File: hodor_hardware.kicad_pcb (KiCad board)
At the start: 2 copper layers, 153.6 x 86 mm, 274 parts, among them J1 Screw_Terminal_01x02, J12 Conn_01x24_Pin, J13 Conn_01x24_Socket, J2 Screw_Terminal_01x06, J3 Screw_Terminal_01x03, J4 USB_C_Receptacle_USB2.0_16P, J5 Screw_Terminal_01x03, J6 Screw_Terminal_01x04, J7 Screw_Terminal_01x02, J8 Screw_Terminal_01x04, J9 Conn_01x04_Pin, K1 FINDER-32.21-x000, K2 FINDER-32.21-x000, Q1 SiS443DN, Q10 BC847BDW1, Q11 2V7002, Q2 BSS138DW, Q3 BSS138DW, Q4 IRLML9301, Q5 BSS138, Q6 BSS138DW, Q7 SiS443DN, Q9 IRLML9301, SW1 SW_RST, SW2 SW_BOOT, T1 GND, T10 V_{BUS}, T11 3V3, T12 5V, T13 5V, T14 V_{BUS}_SENSE, T15 I_SNS, T16 D_FB, T17 D_PWM2, T18 D_PWM1, T19 VC_OUT, T20 V_LDSNS, T21 SCL, T22 VC_CMP, T23 VC_REF, T24 SDA, T25 DRV_EN, T26 DRV_SF, T27 SF_Q, T28 SF_TRG, T29 SF_CLR, T30 ENC_B, T31 ENC_A, T32 GND, T33 3V3, T34 GND, T4 IN2, T5 IN1, T6 V_{DC}_SENSE, T7 IN3, T8 IN4, T9 V_{DC}, U1 ESP32-S3-WROOM-1_N8R2, U10 LM4040DBZ-2.5, U11 MCP6561x-LT, U12 ZXTR2105F, U14 ACS722xLCTR-10AB, U15 TPS2116DRL, U16 MCP23S08-xML, U17 SSD1306, U18 MC33HB2002, U2 TLV62569DBV, U3 74LVC2G14, U4 74LVC2G14, U5 TPS54240DRC, U6 MAX811SEUS-T, U7 74LVC2G14, U8 74LVC1G123, U9 24LC256

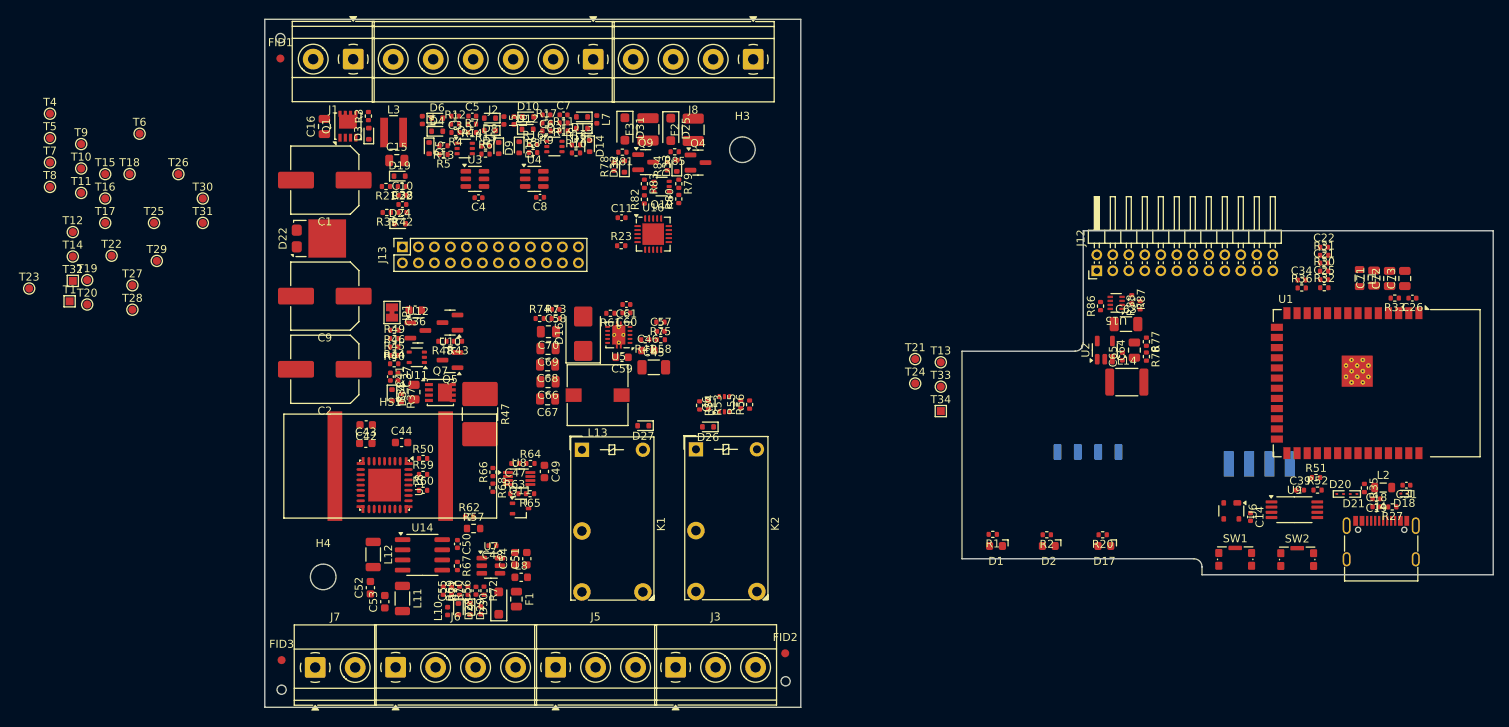
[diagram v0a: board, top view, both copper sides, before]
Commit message: Simplified design (Old version switched to hodor-max)
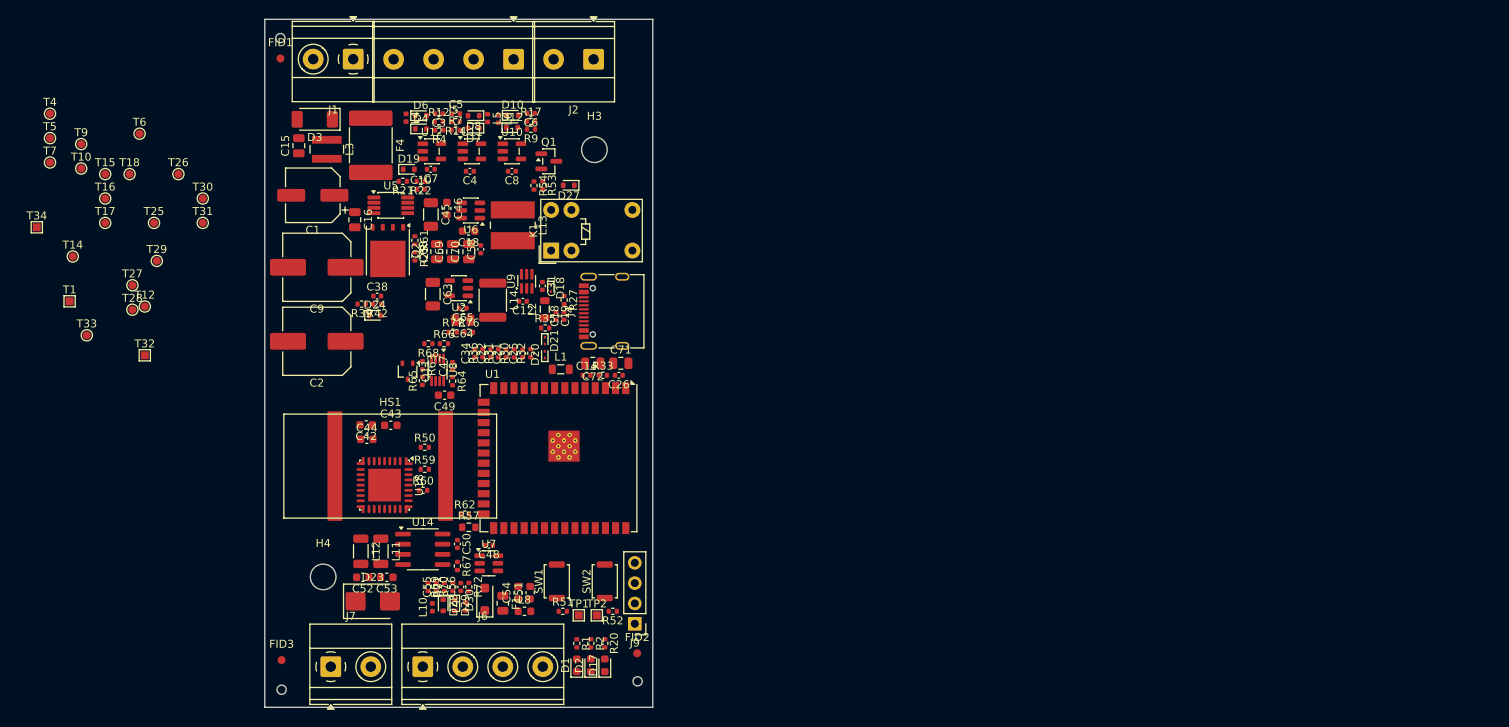
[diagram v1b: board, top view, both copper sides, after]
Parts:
- removed C11, C37, C39: 100nF, Capacitor_SMD:C_0402_1005Metric
- removed C36, C59: 100n/50V, Capacitor_SMD:C_0603_1608Metric
- removed C41: 1u, Capacitor_SMD:C_0402_1005Metric
- removed C57: 6.8nF, Capacitor_SMD:C_0402_1005Metric
- removed C60: 15nF, Capacitor_SMD:C_0402_1005Metric
- removed C61: 10p, Capacitor_SMD:C_0402_1005Metric
- removed C66, C67, C73: 10uF, Capacitor_SMD:C_0805_2012Metric
- removed D11, D14, D5, D9: C5V6, Diode_SMD:D_SOD-523
- removed D13: PESDx, Diode_SMD:D_SOD-523
- removed D15, D26: PMEG3005, Diode_SMD:D_SOD-523
- removed D16: PMEG4050, Diode_SMD:D_SMB
- removed D22: V10PM45, Package_TO_SOT_SMD:TO-277A
- removed D25, D31: PMEG6010, Diode_SMD:D_SOD-123F
- removed D32, D33, D34: BCX84C15V, Diode_SMD:D_SOD-523
- removed F2, F3: 1A, Fuse:Fuse_1210_3225Metric
- removed J12: Conn_01x24_Pin, Connector_PinHeader_2.00mm:PinHeader_2x12_P2.00mm_Horizontal
- removed J13: Conn_01x24_Socket, Connector_PinSocket_2.00mm:PinSocket_2x12_P2.00mm_Vertical
- removed J3: Screw_Terminal_01x03, TerminalBlock_Phoenix:TerminalBlock_Phoenix_MKDS-1,5-3_1x03_P5.00mm_Horizontal
- removed J8: Screw_Terminal_01x04, TerminalBlock_Phoenix:TerminalBlock_Phoenix_MKDS-1,5-4_1x04_P5.00mm_Horizontal
- removed JP1: Jumper_2_Bridged, Jumper:SolderJumper-2_P1.3mm_Bridged_Pad1.0x1.5mm
- removed K2: FINDER-32.21-x000, Relay_THT:Relay_SPDT_Finder_32.21-x000
- removed L7: BLM15AG102, Inductor_SMD:L_0402_1005Metric
- removed Q10: BC847BDW1, Package_TO_SOT_SMD:SOT-363_SC-70-6
- removed Q3, Q6: BSS138DW, Package_TO_SOT_SMD:SOT-363_SC-70-6
- removed Q4, Q9: IRLML9301, Package_TO_SOT_SMD:SOT-23
- removed Q5: BSS138, Package_TO_SOT_SMD:SOT-23
- removed Q7: SiS443DN, Package_SO:Vishay_PowerPAK_1212-8_Single
- removed R10, R13, R15, R16, R18, R5, R6, R8, R81, R85: 2.2k, Resistor_SMD:R_0402_1005Metric
- removed R11, R48, R56: 100R, Resistor_SMD:R_0402_1005Metric
- removed R19, R23, R37, R44, R45, R74, R78, R80, R83, R84, R86, R88: 10k, Resistor_SMD:R_0402_1005Metric
- removed R3, R41: 100k, Resistor_SMD:R_0402_1005Metric
- removed R38: 2k, Resistor_SMD:R_0805_2012Metric
- removed R40, R79, R82: 1k, Resistor_SMD:R_0402_1005Metric
- removed R43, R55: 20k, Resistor_SMD:R_0402_1005Metric
- removed R46: 97.6k, Resistor_SMD:R_0402_1005Metric
- removed R47: 20R/4W, Resistor_SMD:R_2816_7142Metric
- removed R49: 200k, Resistor_SMD:R_0402_1005Metric
- removed R58: 18.2k, Resistor_SMD:R_0402_1005Metric
- removed R73: 52.3k, Resistor_SMD:R_0402_1005Metric
- removed R75: 205k, Resistor_SMD:R_0402_1005Metric
- removed R87: 0R, Resistor_SMD:R_0402_1005Metric
- removed T11: 3V3, TestPoint:TestPoint_Pad_D1.0mm
- removed T13: 5V, TestPoint:TestPoint_Pad_D1.0mm
- removed T19: VC_OUT, TestPoint:TestPoint_Pad_D1.0mm
- removed T20: V_LDSNS, TestPoint:TestPoint_Pad_D1.0mm
- removed T21: SCL, TestPoint:TestPoint_Pad_D1.0mm
- removed T22: VC_CMP, TestPoint:TestPoint_Pad_D1.0mm
- removed T23: VC_REF, TestPoint:TestPoint_Pad_D1.0mm
- removed T24: SDA, TestPoint:TestPoint_Pad_D1.0mm
- removed T8: IN4, TestPoint:TestPoint_Pad_D1.0mm
- removed U15: TPS2116DRL, Package_TO_SOT_SMD:SOT-583-8
- removed U16: MCP23S08-xML, Package_DFN_QFN:QFN-20-1EP_4x4mm_P0.5mm_EP2.7x2.7mm
- removed U17: SSD1306, hodor_footprints:SSD1306_OLED_Horizontal_Reverse
- removed U3, U4: 74LVC2G14, Package_TO_SOT_SMD:SOT-23-6
- added C12: 100n, Capacitor_SMD:C_0402_1005Metric, F.Cu at (80.1, 82.5)
- added C13: 100n/50V, Capacitor_SMD:C_0603_1608Metric, F.Cu at (73.3, 73.7)
- added D23: D_TVS, Diode_SMD:D_SMB, F.Cu at (61.3, 120.0)
- added F4: Polyfuse, Fuse:Fuse_2920_7451Metric, F.Cu at (61.0, 63.0)
- added R25: 100k, Resistor_SMD:R_0402_1005Metric, F.Cu at (66.6, 76.8)
- added TP1: TestPoint_Alt, TestPoint:TestPoint_Pad_1.0x1.0mm, F.Cu at (87.0, 121.7)
- added TP2: TestPoint_Alt, TestPoint:TestPoint_Pad_1.0x1.0mm, F.Cu at (89.3, 121.7)
- C1: value 100uF/50V -> 47uF/50V; footprint Capacitor_SMD:C_Elec_8x10.2 -> Capacitor_SMD:CP_Elec_6.3x5.8
- C14: value 100nF -> 10nF
- C16: value 1u/50V -> 2.2u/25V
- D1, D17, D2: footprint LED_SMD:LED_Kingbright_APA1606_1.6x0.6mm_Horizontal -> LED_SMD:LED_0603_1608Metric
- D3: value BCX84C15V -> PMEG4050EP; footprint Diode_SMD:D_SOD-523 -> Diode_SMD:D_SOD-128
- J2: value Screw_Terminal_01x06 -> Screw_Terminal_01x02; footprint TerminalBlock_Phoenix:TerminalBlock_Phoenix_MKDS-1,5-6_1x06_P5.00mm_Horizontal -> TerminalBlock_Phoenix:TerminalBlock_Phoenix_MKDS-1,5-2_1x02_P5.00mm_Horizontal
- J5: value Screw_Terminal_01x03 -> Screw_Terminal_01x04; footprint TerminalBlock_Phoenix:TerminalBlock_Phoenix_MKDS-1,5-3_1x03_P5.00mm_Horizontal -> TerminalBlock_Phoenix:TerminalBlock_Phoenix_MKDS-1,5-4_1x04_P5.00mm_Horizontal
- J9: footprint hodor_footprints:Conn_Header2.54_1x04_SMD -> Connector_PinHeader_2.54mm:PinHeader_1x04_P2.54mm_Vertical; moved to F.Cu
- K1: value FINDER-32.21-x000 -> G5V-1; footprint Relay_THT:Relay_SPDT_Finder_32.21-x000 -> Relay_THT:Relay_SPDT_Omron_G5V-1
- L13: value 27uH -> 6.8uH; footprint Inductor_SMD:L_Wuerth_WE-PD-Typ-7345 -> Inductor_SMD:L_Wuerth_WE-PD2-Typ-MS
- L3: value 4.7uH/4A -> 2.2uH/4A
- Q1: value SiS443DN -> BSS138; footprint Package_SO:Vishay_PowerPAK_1212-8_Single -> Package_TO_SOT_SMD:SOT-23
- Q2: value BSS138DW -> FDMS86550; footprint Package_TO_SOT_SMD:SOT-363_SC-70-6 -> Package_TO_SOT_SMD:TDSON-8-1
- R33: value 100k -> 10k
- R51, R52: value 2.2k -> 4.7k
- R61: value 18.2k -> 13.7k
- SW1, SW2: footprint Button_Switch_SMD:SW_SPST_CK_KMS2xxG -> Button_Switch_SMD:SW_Push_SPST_NO_Alps_SKRK
- U1: footprint RF_Module:ESP32-S3-WROOM-1 -> RF_Module:ESP32-S3-WROOM-1U
- U10: value LM4040DBZ-2.5 -> SN74LVC1G14DBV; footprint Package_TO_SOT_SMD:SOT-23 -> Package_TO_SOT_SMD:SOT-23-5
- U11: value MCP6561x-LT -> SN74LVC1G14DBV; footprint Package_TO_SOT_SMD:SOT-353_SC-70-5 -> Package_TO_SOT_SMD:SOT-23-5
- U12: value ZXTR2105F -> SN74LVC1G14DBV; footprint Package_TO_SOT_SMD:SOT-23 -> Package_TO_SOT_SMD:SOT-23-5
- U5: value TPS54240DRC -> LM74610-Q1; footprint Package_SON:Texas_DRC0010J_ThermalVias -> Package_SO:VSSOP-8_3x3mm_P0.65mm
- U6: value MAX811SEUS-T -> LMR51430; footprint Package_TO_SOT_SMD:SOT-143 -> Package_TO_SOT_SMD:SOT-23-6
- U9: value 24LC256 -> LM66100DCK; footprint Package_SO:TSSOP-8_4.4x3mm_P0.65mm -> Package_TO_SOT_SMD:SOT-363_SC-70-6
- moved T34 115.3 mm to (19.3, 73.2)
- moved C31 110.8 mm to (82.5, 80.5), turned to -90 degrees
- moved D18 109.7 mm to (83.5, 80.8), turned to -90 degrees
- moved L2 107.1 mm to (82.8, 83.4), turned to 90 degrees
- moved T33 106.9 mm to (25.6, 86.7)
- moved R27 106.7 mm to (85.2, 82.3), turned to -90 degrees
- moved C19 105.1 mm to (84.2, 84.3), turned to -90 degrees
- moved C22 105.0 mm to (76.0, 88.9), turned to 90 degrees
- moved R35 104.3 mm to (82.8, 85.8), turned to 0 degrees
- moved C18 104.3 mm to (85.2, 84.3), turned to 90 degrees
- moved R31 104.0 mm to (77.0, 89.0), turned to 90 degrees
- moved C34 103.7 mm to (74.1, 89.0), turned to 90 degrees
- moved D21 102.9 mm to (82.8, 87.4), turned to -90 degrees
- moved C21 102.9 mm to (78.0, 89.0), turned to 90 degrees
- moved U1 102.7 mm to (84.5, 102.1)
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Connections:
- C10 pad 1: /Controllerboard/ADC_CH2 -> /Controllerboard/V_{DC}_SENSE
- C14 pad 1: GNDD -> GND
- C14 pad 2: VD3V3 -> Net-(U1-EN)
- C16 pad 1: Net-(D3-K) -> Net-(U5-V_{CAP}L)
- C16 pad 2: GND -> Net-(U5-V_{CAP}H)
- C18 pad 1: 5V_USB -> Net-(C18-Pad1)
- C18 pad 2: GNDD -> GND
- C19 pad 1: GNDD -> GND
- C19 pad 2: 5V_USB -> Net-(C18-Pad1)
- C21 pad 1: GNDD -> GND
- C22 pad 1: GNDD -> GND
- C25 pad 1: GNDD -> GND
- C26 pad 1: GNDD -> GND
- C31 pad 2: GNDD -> GND
- C34 pad 1: GNDD -> GND
- C38 pad 1: /Controllerboard/ADC_CH1 -> /Controllerboard/V_{BUS}_SENSE
- C63 pad 1: Net-(U2-EN) -> +5V
- C63 pad 2: GNDD -> GND
- C64 pad 2: GNDD -> GND
- C65 pad 2: GNDD -> GND
- C7 pad 1: Net-(C7-Pad1) -> +3V3
- C71 pad 2: GNDD -> GND
- C72 pad 2: GNDD -> GND
- D1 pad 1: GNDD -> GND
- D17 pad 1: GNDD -> GND
- D18 pad 1: GNDD -> GND
- D19 pad 1: /Controllerboard/ADC_CH2 -> /Controllerboard/V_{DC}_SENSE
- D2 pad 1: GNDD -> GND
- D20 pad 1: GNDD -> GND
- D21 pad 1: GNDD -> GND
- D24 pad 1: /Controllerboard/ADC_CH1 -> /Controllerboard/V_{BUS}_SENSE
- D3 pad 2: Net-(D3-A) -> GND
- J2 pad 1: Net-(D13-K) -> Net-(J2-Pin_1)
- J2 pad 2: Net-(D10-K) -> Net-(J2-Pin_2)
- J4 pad A1: GNDD -> GND
- J4 pad A12: GNDD -> GND
- J4 pad B1: GNDD -> GND
- J4 pad B12: GNDD -> GND
- J5 pad 1: Net-(J5-Pin_1) -> Net-(D10-K)
- J5 pad 2: Net-(J5-Pin_2) -> Net-(D8-K)
- J5 pad 3: Net-(J5-Pin_3) -> Net-(D6-K)
- J9 pad 1: GNDD -> GND
- J9 pad 4: VD3V3 -> +3V3
- L1 pad 1: VD3V3 -> +3V3
- L13 pad 1: Net-(D16-K) -> Net-(U6-SW)
- L2 pad 1: 5V_USB -> Net-(C18-Pad1)
- Q1 pad 1: Net-(D3-K) -> Net-(Q1-G)
- Q1 pad 2: Net-(D3-K) -> GND
- Q1 pad 3: Net-(D3-K) -> Net-(D27-A)
- Q2 pad 1: GND -> VDC
- Q2 pad 2: Net-(Q2A-G) -> VDC
- Q2 pad 3: Net-(D7-A) -> VDC
- Q2 pad 4: GND -> Net-(Q2-G)
- Q2 pad 5: Net-(Q2B-G) -> VBUS
- R21 pad 1: /Controllerboard/ADC_CH2 -> /Controllerboard/V_{DC}_SENSE
- R22 pad 2: /Controllerboard/ADC_CH2 -> /Controllerboard/V_{DC}_SENSE
- R27 pad 2: GNDD -> GND
- R30 pad 1: Net-(J12-Pin_22) -> /Controllerboard/ADC_DRV_FB
- R31 pad 1: Net-(J12-Pin_21) -> /Controllerboard/ADC_I_{SENSE}
- R32 pad 1: Net-(J12-Pin_23) -> /Controllerboard/V_{BUS}_SENSE
- R33 pad 2: GNDD -> Net-(U1-3V3)
- R35 pad 2: GNDD -> GND
- R36 pad 1: Net-(J12-Pin_24) -> /Controllerboard/V_{DC}_SENSE
- R39 pad 1: /Controllerboard/ADC_CH1 -> /Controllerboard/V_{BUS}_SENSE
- R42 pad 2: /Controllerboard/ADC_CH1 -> /Controllerboard/V_{BUS}_SENSE
- R53 pad 1: Net-(Q6B-G) -> Net-(Q1-G)
- R54 pad 1: Net-(Q6B-G) -> Net-(Q1-G)
- R54 pad 2: /Peripherals/REL_CTRL_1 -> /Controllerboard/REL_CTRL1
- R57 pad 1: /Controllerboard/ADC_CH3 -> /Controllerboard/ADC_DRV_FB
- R61 pad 1: Net-(C60-Pad2) -> GND
- R61 pad 2: Net-(U5-COMP) -> Net-(U6-FB)
- R77 pad 1: GNDD -> GND
- SW1 pad 1: GNDD -> GND
- SW1 pad 2: Net-(U6-~{MR}) -> Net-(U1-EN)
- SW2 pad 1: GNDD -> GND
- T14 pad 1: /Controllerboard/ADC_CH1 -> /Controllerboard/V_{BUS}_SENSE
- T15 pad 1: /Controllerboard/ADC_CH4 -> /Controllerboard/ADC_I_{SENSE}
- T16 pad 1: /Controllerboard/ADC_CH3 -> /Controllerboard/ADC_DRV_FB
- T34 pad 1: GNDD -> GND
- T4 pad 1: /Peripherals/INPUT_2 -> /Controllerboard/INPUT_2
- T5 pad 1: /Peripherals/INPUT_1 -> /Controllerboard/INPUT_1
- T6 pad 1: /Controllerboard/ADC_CH2 -> /Controllerboard/V_{DC}_SENSE
- T7 pad 1: /Peripherals/INPUT_3 -> /Controllerboard/INPUT_3
- U1 pad 1: GNDD -> GND
- U1 pad 10: unconnected-(U1-IO17-Pad10) -> /Controllerboard/INPUT_1
- U1 pad 11: unconnected-(U1-IO18-Pad11) -> /Controllerboard/INPUT_2
- U1 pad 15: unconnected-(U1-IO3-Pad15) -> /Controllerboard/REL_CTRL1
- U1 pad 16: /Controllerboard/D_~{SF} -> /Controllerboard/DRV_~{SF}
- U1 pad 17: /Controllerboard/SPI_~{CS1} -> unconnected-(U1-IO9-Pad17)
- U1 pad 18: /Controllerboard/SPI_~{CS0} -> /Controllerboard/~{CS0}
- U1 pad 19: /Controllerboard/SPI_MISO -> /Controllerboard/MISO
- U1 pad 20: /Controllerboard/SPI_SCK -> /Controllerboard/SCK
- U1 pad 21: /Controllerboard/SPI_MOSI -> /Controllerboard/MOSI
- U1 pad 24: /Controllerboard/D_PWM1 -> /Controllerboard/DRV_PWM1
- U1 pad 25: /Controllerboard/D_PWM2 -> /Controllerboard/DRV_PWM2
- U1 pad 26: /Controllerboard/D_EN -> /Controllerboard/DRV_EN
- U1 pad 28: /Controllerboard/ENC_A -> /Controllerboard/ENCODER_A
- U1 pad 29: /Controllerboard/ENC_B -> /Controllerboard/ENCODER_B
- U1 pad 32: /Controllerboard/IO_MUX_INT -> /Controllerboard/INPUT_3
- U1 pad 33: /Controllerboard/IO_MUX_~{RST} -> unconnected-(U1-IO40-Pad33)
- U1 pad 34: /Controllerboard/SF_~{CLR} -> /Controllerboard/SAFETY_~{CLR}
- U1 pad 35: /Controllerboard/SF_TRG -> /Controllerboard/SAFETY_TRIG
- U1 pad 40: GNDD -> GND
- U1 pad 41: GNDD -> GND
- U10 pad 1: Net-(U10-K) -> unconnected-(U10-NC-Pad1)
- U10 pad 2: GND -> Net-(C6-Pad1)
- U10 pad 3: unconnected-(U10-NC-Pad3) -> GND
- U11 pad 1: Net-(R48-Pad2) -> unconnected-(U11-NC-Pad1)
- U11 pad 2: GND -> Net-(C5-Pad1)
- U11 pad 3: Net-(U11-+) -> GND
- U11 pad 4: Net-(U10-K) -> /Controllerboard/INPUT_2
- U11 pad 5: Net-(U11-V+) -> +3V3
- U12 pad 1: GND -> unconnected-(U12-NC-Pad1)
- U12 pad 2: Net-(U11-V+) -> Net-(C3-Pad1)
- U12 pad 3: VBUS -> GND
- U14 pad 7: /Controllerboard/ADC_CH4 -> /Controllerboard/ADC_I_{SENSE}
- U18 pad 10: /Controllerboard/ADC_CH3 -> /Controllerboard/ADC_DRV_FB
- U2 pad 1: Net-(U2-EN) -> +5V
- U2 pad 2: GNDD -> GND
- U2 pad 4: Net-(U2-EN) -> +5V
- U5 pad 1: Net-(U5-BOOT) -> Net-(U5-V_{CAP}L)
- U5 pad 2: VDC -> Net-(Q2-G)
- U5 pad 3: Net-(U5-EN) -> unconnected-(U5-NC-Pad3)
- U5 pad 4: Net-(U5-SS/TR) -> VDC
- U5 pad 5: Net-(U5-RT/CLK) -> unconnected-(U5-NC-Pad5)
- U5 pad 6: unconnected-(U5-PWRGD-Pad6) -> Net-(Q2-G)
- U5 pad 7: Net-(U5-VSENSE) -> Net-(U5-V_{CAP}H)
- U5 pad 8: Net-(U5-COMP) -> VBUS
- U6 pad 1: GNDD -> GND
- U6 pad 2: Net-(U1-EN) -> Net-(U6-SW)
- U6 pad 3: Net-(U6-~{MR}) -> VDC
- U6 pad 4: VD3V3 -> Net-(U6-FB)
- U9 pad 1: GNDD -> 5V_USB
- U9 pad 2: GNDD -> GND
- U9 pad 3: GNDD -> +5V
- U9 pad 4: GNDD -> unconnected-(U9-NC-Pad4)
- U9 pad 5: /Controllerboard/SDA -> GND
- U9 pad 6: /Controllerboard/SCL -> +5V
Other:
- board size 153.6 x 86 mm -> 48.5 x 86 mm
- board text removed: "-"
- board text removed: "01.02.2017"
- board text removed: "044934011"
- board text removed: "044934055"
- board text removed: "1"
- board text removed: "1/1"
- board text removed: "1:1"
- board text removed: "2"
- board text removed: "3"
- board text removed: "4"
- board text removed: "449-340-11"
- board text removed: "449-340-56"
- board text removed: "5"
- board text removed: "6"
- board text removed: "7"
- board text removed: "8"
- board text removed: "A"
- board text removed: "B"
- board text removed: "BENENNUNG"
- board text removed: "BESCHREIBUNG"
- board text removed: "Bearb."
- board text removed: "Benennung"
- board text removed: "Blatt"
- board text removed: "D.Haas"
- board text removed: "Datum"
- board text removed: "Gepr."
- board text removed: "Gewerbegebiet D-54552 Mehren"
- board text removed: "Housing: Apra-Rail DB4"
- board text removed: "J.Schmitz"
- board text removed: "Klemmen"
- board text removed: "MENGE"
- board text removed: "Material:"
- board text removed: "Name"
- board text removed: "POS-NR."
- board text removed: "Progr."
- board text removed: "SCHNITT A-A"
- board text removed: "SCHNITT B-B"
- board text removed: "Unterschale 4DB"
- board text removed: "Unterschale DB 3"
- board text removed: "Version"
- board text removed: "Zeichnungsnummer"
- board text removed: "apra-norm Elektromechanik GmbH"
- board text removed: "apraRail DB4"
- board text removed: "neu erstellt"

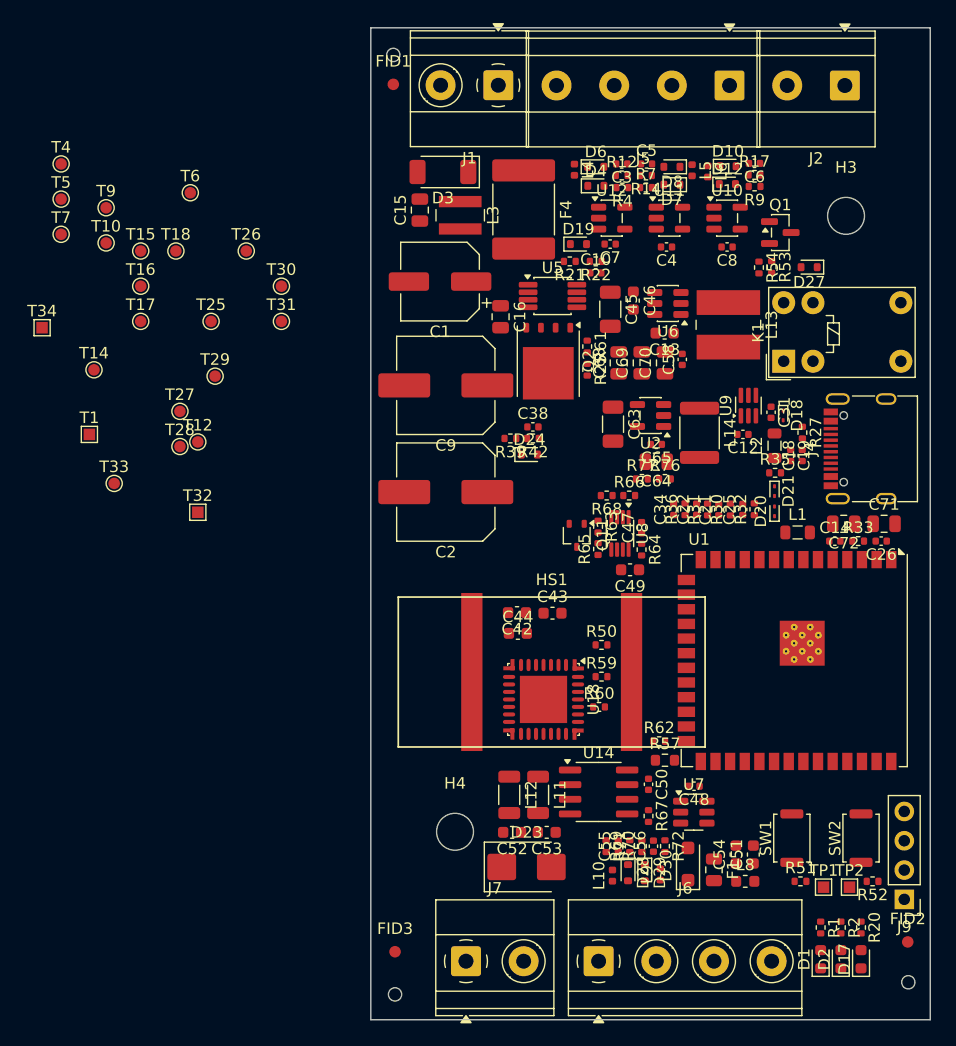
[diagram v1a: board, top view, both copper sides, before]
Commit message: All nets connected
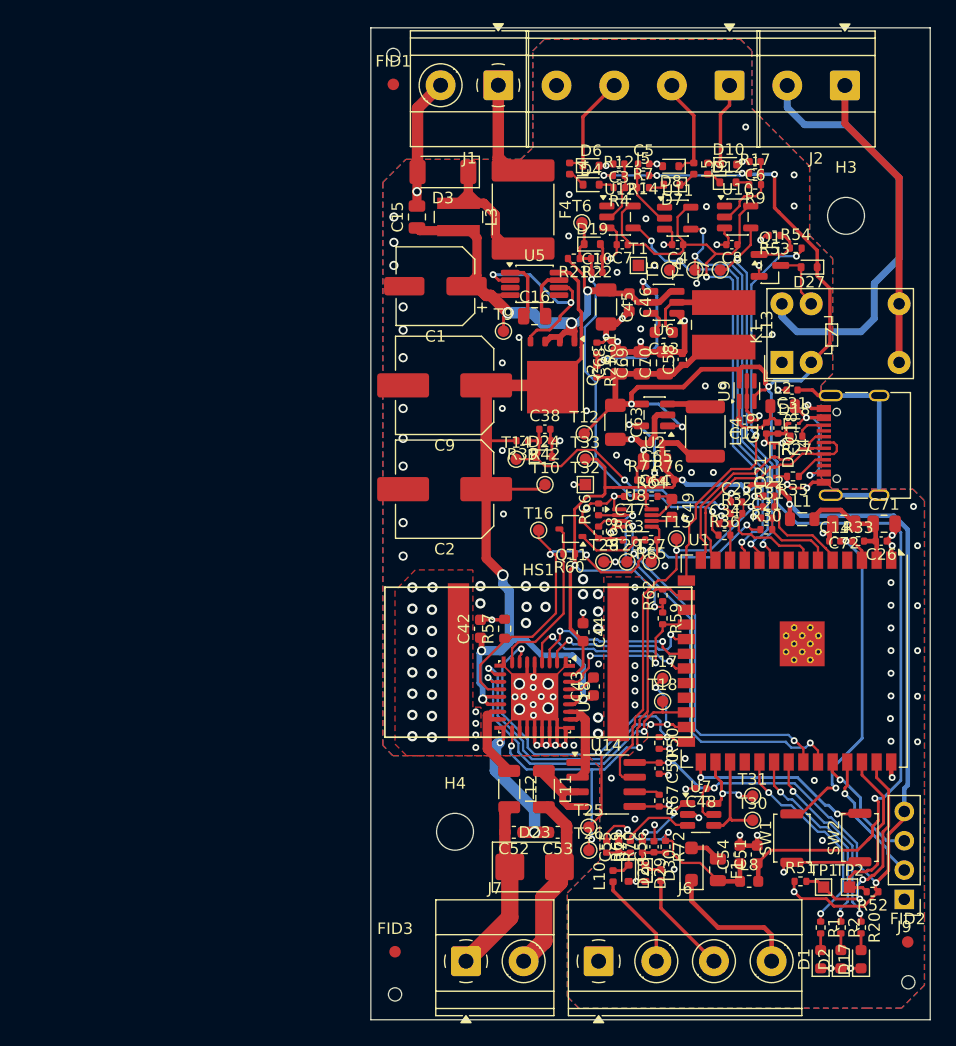
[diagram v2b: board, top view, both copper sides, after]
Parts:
- removed T34: GND, TestPoint:TestPoint_Pad_1.0x1.0mm
- moved T30 61.7 mm to (80.9, 115.9)
- moved T26 59.8 mm to (66.7, 118.5)
- moved T31 58.0 mm to (80.9, 113.8)
- moved T18 57.5 mm to (73.1, 105.6)
- moved T7 57.2 mm to (78.1, 68.2), turned to 90 degrees
- moved T4 55.7 mm to (75.9, 68.2), turned to 90 degrees
- moved T17 54.8 mm to (73.1, 103.6)
- moved T25 54.7 mm to (66.7, 116.5)
- moved T5 53.1 mm to (73.7, 68.2), turned to 90 degrees
- moved T15 52.7 mm to (74.3, 91.5)
- moved T1 49.8 mm to (71.0, 67.8)
- moved T10 43.4 mm to (62.9, 86.8)
- moved T27 42.9 mm to (72.1, 93.5)
- moved T33 40.9 mm to (66.4, 84.6)
- moved T16 40.5 mm to (62.4, 90.8)
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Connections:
- C18 pad 1: Net-(C18-Pad1) -> 5V_USB
- C19 pad 2: Net-(C18-Pad1) -> 5V_USB
- C64 pad 1: VD3V3 -> +3V3
- C65 pad 1: VD3V3 -> +3V3
- L14 pad 2: VD3V3 -> +3V3
- L2 pad 1: Net-(C18-Pad1) -> 5V_USB
- R51 pad 1: Net-(U1-3V3) -> +3V3
- R52 pad 1: Net-(U1-3V3) -> +3V3
- R76 pad 2: VD3V3 -> +3V3
- T33 pad 1: VD3V3 -> +3V3
- U1 pad 10: /Controllerboard/INPUT_1 -> /Controllerboard/INPUT_2
- U1 pad 11: /Controllerboard/INPUT_2 -> /Controllerboard/INPUT_1
- U1 pad 22: /Controllerboard/LED_CONN -> unconnected-(U1-IO14-Pad22)
- U1 pad 31: unconnected-(U1-IO38-Pad31) -> /Controllerboard/LED_ACTIVE
- U1 pad 32: /Controllerboard/INPUT_3 -> /Controllerboard/LED_STATUS
- U1 pad 33: unconnected-(U1-IO40-Pad33) -> /Controllerboard/LED_CONN
- U1 pad 8: /Controllerboard/LED_ACTIVE -> unconnected-(U1-IO15-Pad8)
- U1 pad 9: /Controllerboard/LED_STATUS -> /Controllerboard/INPUT_3
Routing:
- net GND: track 0.00 -> 199.0 mm, vias 0 -> 170
- net +3V3: track 0.00 -> 196.7 mm, vias 0 -> 10
- net +5V: track 0.00 -> 150.7 mm, vias 0 -> 8
- net VBUS: track 0.00 -> 77.9 mm, vias 0 -> 4
- net VDC: track 0.00 -> 45.1 mm, vias 0 -> 3
- net /Controllerboard/ADC_DRV_FB: track 0.00 -> 42.2 mm, vias 0 -> 4
- net /Controllerboard/SAFETY_TRIG: track 0.00 -> 40.7 mm, vias 0 -> 3
- net /Controllerboard/DRV_~{SF}: track 0.00 -> 39.0 mm, vias 0 -> 3
- net /Controllerboard/INPUT_1: track 0.00 -> 38.9 mm, vias 0 -> 3
- net /Controllerboard/V_{DC}_SENSE: track 0.00 -> 37.8 mm, vias 0 -> 2
- net Net-(J2-Pin_2): track 0.00 -> 37.4 mm
- net /Controllerboard/INPUT_2: track 0.00 -> 36.2 mm, vias 0 -> 3
- net /Controllerboard/DRV_EN: track 0.00 -> 36.0 mm, vias 0 -> 3
- net /Controllerboard/SAFETY_~{CLR}: track 0.00 -> 35.4 mm, vias 0 -> 3
- net /Controllerboard/REL_CTRL1: track 0.00 -> 35.1 mm, vias 0 -> 2
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- added copper zone on B.Cu, net GND
- added copper zone on F.Cu, net GND

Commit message: Finalized Layout
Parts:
- added G***: LOGO, LOGO, B.Cu at (53.4, 79.5)
- added REF**: KiCad-Logo_5mm_SilkScreen, Symbol:KiCad-Logo_5mm_SilkScreen, F.Cu at (50.7, 116.2)
- added REF**: OSHW-Logo_5.7x6mm_SilkScreen, Symbol:OSHW-Logo_5.7x6mm_SilkScreen, F.Cu at (92.8, 66.3)
- C19: renamed from C31; value 10nF/50V -> 10nF/25V
- C22: renamed from C12; value 100n -> 100nF
- C29: renamed from C49; value 2.2u/10V -> 2.2u/25V; footprint Capacitor_SMD:C_0603_1608Metric -> Capacitor_SMD:C_0805_2012Metric
- R14: renamed from R42; value 2k -> 2.2k
- R39: renamed from R51; value 4.7k -> 5.1k
- R40: renamed from R52; value 4.7k -> 5.1k
- R8: renamed from R22; value 2k -> 2.2k
- moved C29 0.20 mm to (74.0, 89.0)
- renumbered C3 to C1, C16 to C10, C45 to C11, C46 to C12, C68 to C14, C69 to C15, C58 to C16, C70 to C17, C9 to C18, C5 to C2, C38 to C20, C63 to C21, C19 to C23, C18 to C24, C65 to C25, C64 to C26, C2 to C27, C47 to C28, C6 to C3, C25 to C30, C21 to C31, C22 to C32, C34 to C33, C72 to C34, C14 to C35, C71 to C36, C26 to C37, C42 to C38, C44 to C39, C15 to C4, C43 to C40, C50 to C41, C48 to C42, C52 to C43, C53 to C44, C55 to C45, C56 to C46, C54 to C47, C51 to C48, C7 to C5, C4 to C6, C8 to C7, C1 to C8, C10 to C9, D6 to D1, D18 to D10, D24 to D11, D20 to D12, D21 to D13, D23 to D14, D28 to D15, D29 to D16, D30 to D17, D1 to D18, D2 to D19, D8 to D2, D17 to D20, D10 to D3, D3 to D4, D4 to D5, D7 to D6, D12 to D7, D19 to D8, D27 to D9, F4 to F1, F1 to F2, FID3 to FID2, FID2 to FID3, H7 to H1, H3 to H2, H4 to H3, H8 to H4, H6 to H5, J5 to J2, J2 to J3, J9 to J5, J7 to J6, J6 to J7, L4 to L1, L11 to L10, L9 to L11, L10 to L12, L8 to L13, L5 to L2, L6 to L3, L3 to L4, L13 to L5, L2 to L6, L14 to L7, L1 to L8, L12 to L9, Q11 to Q3, R4 to R1, R54 to R10, R61 to R11, R25 to R12, R39 to R13, R27 to R15, R77 to R16, R76 to R17, R35 to R18, R66 to R19, R12 to R2, R64 to R20, R32 to R21, R31 to R22, R68 to R23, R63 to R24, R65 to R25, R36 to R26, R30 to R27, R33 to R28, R60 to R29, R14 to R3, R62 to R30, R57 to R31, R59 to R32, R50 to R33, R67 to R34, R71 to R35, R69 to R36, R70 to R37, R72 to R38, R7 to R4, R1 to R41, R2 to R42, R20 to R43, R9 to R5, R17 to R6, R21 to R7, R53 to R9, T6 to T1, T32 to T11, T16 to T12, T15 to T13, T28 to T14, T29 to T15, T27 to T16, T31 to T19, T1 to T2, T25 to T20, T30 to T21, T26 to T22, T5 to T3, T7 to T5, T9 to T6, T12 to T7, T14 to T8, T33 to T9, U12 to U1, U18 to U10, U14 to U11, U7 to U12, U11 to U2, U10 to U3, U5 to U4, U6 to U5, U9 to U6, U2 to U7, U1 to U9
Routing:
- net +3V3: track 196.7 -> 196.4 mm, vias 10 -> 9
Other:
- board text added: "+12..24V"
- board text added: "+5V"
- board text added: "3V3"
- board text added: "5V"
- board text added: "A"
- board text added: "ADC_FB"
- board text added: "B"
- board text added: "BOOT"
- board text added: "CLR"
- board text added: "D_EN"
- board text added: "D_SF"
- board text added: "ENC_A"
- board text added: "ENC_B"
- board text added: "GND"
- board text added: "HODOR r.00 - 03/2026"
- board text added: "I1"
- board text added: "I2"
- board text added: "I3"
- board text added: "IN_1"
- board text added: "IN_2"
- board text added: "IN_3"
- board text added: "I_SNS"
- board text added: "MOT_A"
- board text added: "MOT_B"
- board text added: "PWM"
- board text added: "RC"
- board text added: "REL_COM"
- board text added: "REL_NO"
- board text added: "RESET"
- board text added: "Rx"
- board text added: "SCL"
- board text added: "SDA"
- board text added: "TRG"
- board text added: "Tx"
- board text added: "VBUS"
- board text added: "VB_SNS"
- board text added: "VDC"
- board text added: "V_SNS"
